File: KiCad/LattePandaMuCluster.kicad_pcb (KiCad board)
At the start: 2 copper layers, 203.2 x 170.2 mm, 723 parts, among them J1 ATX-24, J10 Bus_M.2_Socket_M, J11 Bus_M.2_Socket_M, J12 Bus_M.2_Socket_M, J13 Bus_M.2_Socket_M, J14 Bus_M.2_Socket_M, J15 Conn_01x04, J16 Conn_01x05, J17 Conn_01x04, J18 Conn_01x04, J19 RJ45_LED_Shielded_x2, J2 Conn_02x04_Top_Bottom, J20 RJE361882415, J21 RJ45_LED_Shielded_x2, J22 USB3_A_Stacked, J23 USB3_IDC, J24 Conn_01x04, J25 Conn_01x05, J26 HDMI_A, J27 JACK-USBE-20PINTL, J3 SFF-8087, J4 SFF-8087, J5 SATA, J6 Bus_M.2_Socket_E, J7 Bus_M.2_Socket_E, J8 Bus_PCI_Express_x4, J9 Bus_PCI_Express_x4, M1 Fan_4pin, M10 Fan_4pin, M2 Fan_4pin, M3 Fan_4pin, M4 Fan_4pin, M5 Fan_4pin, M6 Fan_4pin, M7 Fan_4pin, M8 Fan_4pin, M9 Fan_4pin, Q1 2N7002, Q2 2N7002, Q3 2N7002, U1 ZD25Q64BSIGT, U10 H5VU25U, U11 H5VU25U, U12 KTI226V, U13 KTI226V, U14 ZD25Q64BSIGT, U15 ZD25Q64BSIGT, U16 H5VU25U, U17 H5VU25U, U18 H5VU25U, U19 H5VU25U, U2 ZD25Q64BSIGT, U20 KTI226V, U21 KTI226V, U22 ZD25Q64BSIGT, U23 ZD25Q64BSIGT, U24 H5VU25U, U25 H5VU25U, U26 KTI226V, U27 ZD25Q64BSIGT, U28 H5VU25U, U29 H5VU25U, U3 ZD25Q64BSIGT, U30 H5VU25U, U31 H5VU25U, U32 H5VU25U, U33 H5VU25U, U34 H5VU25U, U35 H5VU25U, U36 H5VU25U, U37 H5VU25U, U38 H5VU25U, U39 H5VU25U, U4 ZD25Q64BSIGT, U40 TPS65987DDJRSHR, U41 H5VU25U, U42 H5VU25U, U43 ZD25Q64BSIGT, U44 H5VU25U, U5 ZD25Q64BSIGT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

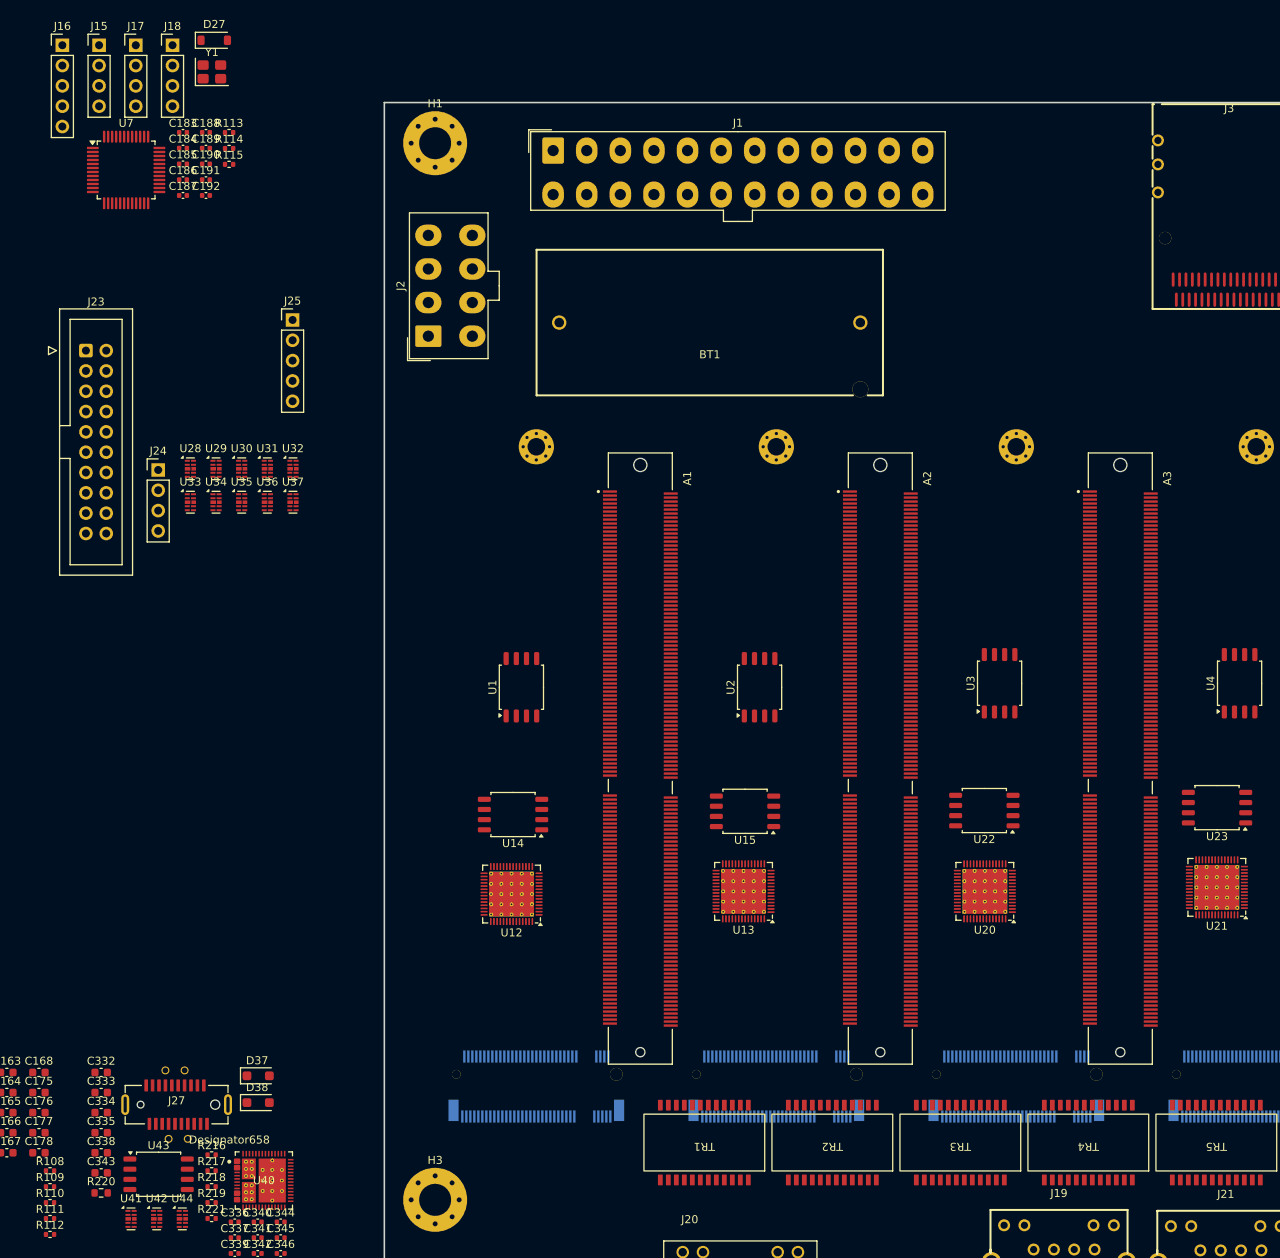
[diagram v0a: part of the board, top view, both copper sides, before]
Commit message: Fix more footprint issues, continue laying out components
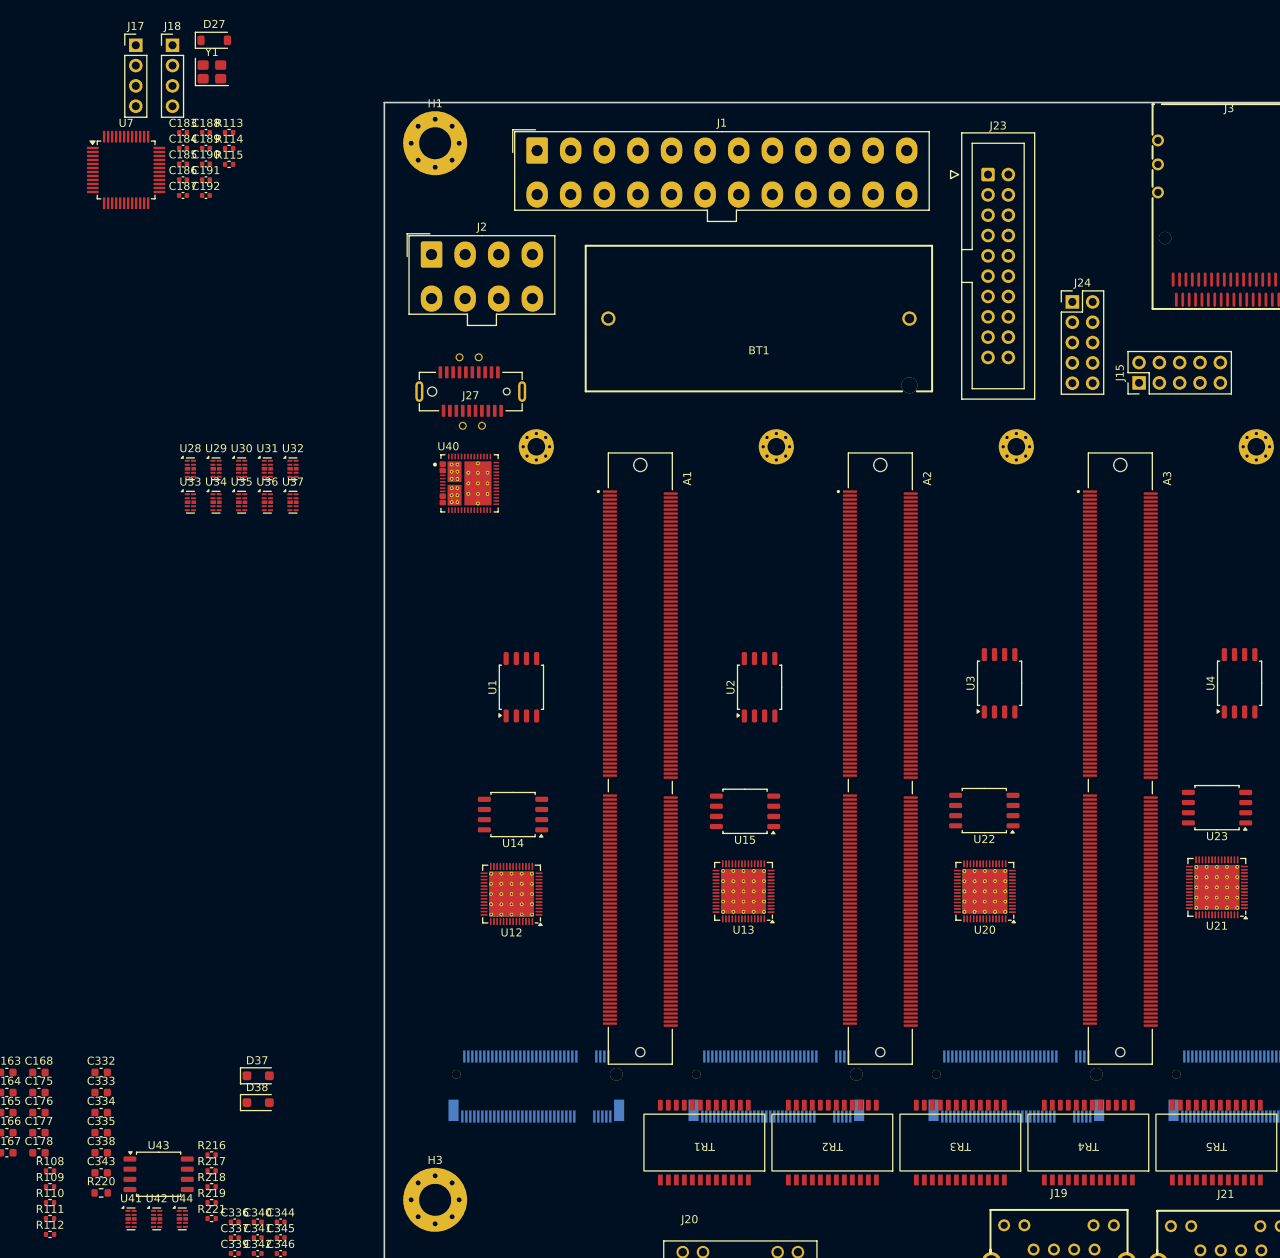
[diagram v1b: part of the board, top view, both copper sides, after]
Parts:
- removed J16, J25: Conn_01x05, Connector_PinHeader_2.54mm:PinHeader_1x05_P2.54mm_Vertical
- J15, J24: value Conn_01x04 -> Conn_02x05_Odd_Even; footprint Connector_PinHeader_2.54mm:PinHeader_1x04_P2.54mm_Vertical -> Connector_PinHeader_2.54mm:PinHeader_2x05_P2.54mm_Vertical
- moved J15 136.7 mm to (194.3, 85.0), turned to 90 degrees
- moved J24 116.2 mm to (186.0, 74.9)
- moved J23 114.9 mm to (175.5, 59.0)
- moved J27 96.4 mm to (110.8, 86.1), turned to 180 degrees
- moved U40 90.9 mm to (110.6, 97.6)
- moved J2 10.2 mm to (105.9, 69.0), turned to 0 degrees
- moved BT1 6.16 mm to (146.8, 77.0)
- moved J1 2.00 mm to (119.1, 56.0)
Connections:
- net /Module 1/TYPE_C_HEADER.SBU2 renamed /Module 1/TYPE_C_HEADER.SBU1
- C189 pad 2: Net-(J15-Pin_3) -> Net-(J15-Pin_5)
- C191 pad 2: Net-(J16-Pin_3) -> Net-(J15-Pin_6)
- J15 pad 2: /Module 1/HDD_LED -> Net-(J15-Pin_2)
- J15 pad 3: Net-(J15-Pin_3) -> /Module 1/HDD_LED
- J15 pad 4: GND -> /PSU/PWR_OK
- J22 pad SH: (no net) -> GND
- J24 pad 2: /Module 5/FUSB_D- -> +5VSB
- J24 pad 3: /Module 5/FUSB_D+ -> /Module 4/FUSB_D-
- J24 pad 4: GND -> /Module 5/FUSB_D-
- R113 pad 2: Net-(J16-Pin_1) -> Net-(J15-Pin_1)
- R114 pad 2: Net-(J15-Pin_1) -> Net-(J15-Pin_2)
- U7 pad 11: Net-(J15-Pin_3) -> Net-(J15-Pin_5)
- U7 pad 12: Net-(J16-Pin_3) -> Net-(J15-Pin_6)

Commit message: Place STM32 and fix cpu fan headers
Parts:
- M1, M3, M5, M7, M9: footprint Connector:FanPinHeader_1x04_P2.54mm_Vertical -> Connector_JST:JST_PH_B4B-PH-K_1x04_P2.00mm_Vertical
- moved J18 166.4 mm to (236.0, 78.9)
- moved M3 165.0 mm to (139.5, 102.0), turned to 90 degrees
- moved U7 162.3 mm to (227.8, 84.8)
- moved J17 146.1 mm to (209.6, 82.5), turned to 90 degrees

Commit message: Place fan headers, adjust other components'
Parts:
- moved M10 415.4 mm to (297.5, 60.1), turned to 90 degrees
- moved M8 404.8 mm to (273.5, 60.1), turned to 90 degrees
- moved M9 368.2 mm to (260.5, 96.0), turned to -90 degrees
- moved M7 348.8 mm to (230.5, 96.0), turned to -90 degrees
- moved M1 243.7 mm to (140.5, 96.0), turned to -90 degrees
- moved M5 220.7 mm to (200.5, 96.0), turned to -90 degrees
- moved M6 216.0 mm to (191.5, 60.0), turned to 90 degrees
- moved M2 207.0 mm to (106.5, 177.1), turned to 90 degrees
- moved M4 135.5 mm to (115.0, 60.0), turned to 90 degrees
- moved J27 83.8 mm to (194.6, 85.0)
- moved J2 51.5 mm to (157.4, 69.0)
- moved J15 48.6 mm to (241.8, 74.5)
- moved J17 48.6 mm to (257.1, 72.0)
- moved M3 31.6 mm to (170.5, 96.0), turned to -90 degrees
- moved BT1 23.5 mm to (123.3, 75.5)
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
